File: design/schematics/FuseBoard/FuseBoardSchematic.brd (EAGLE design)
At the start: 114.3 x 88.9 mm, 11 parts

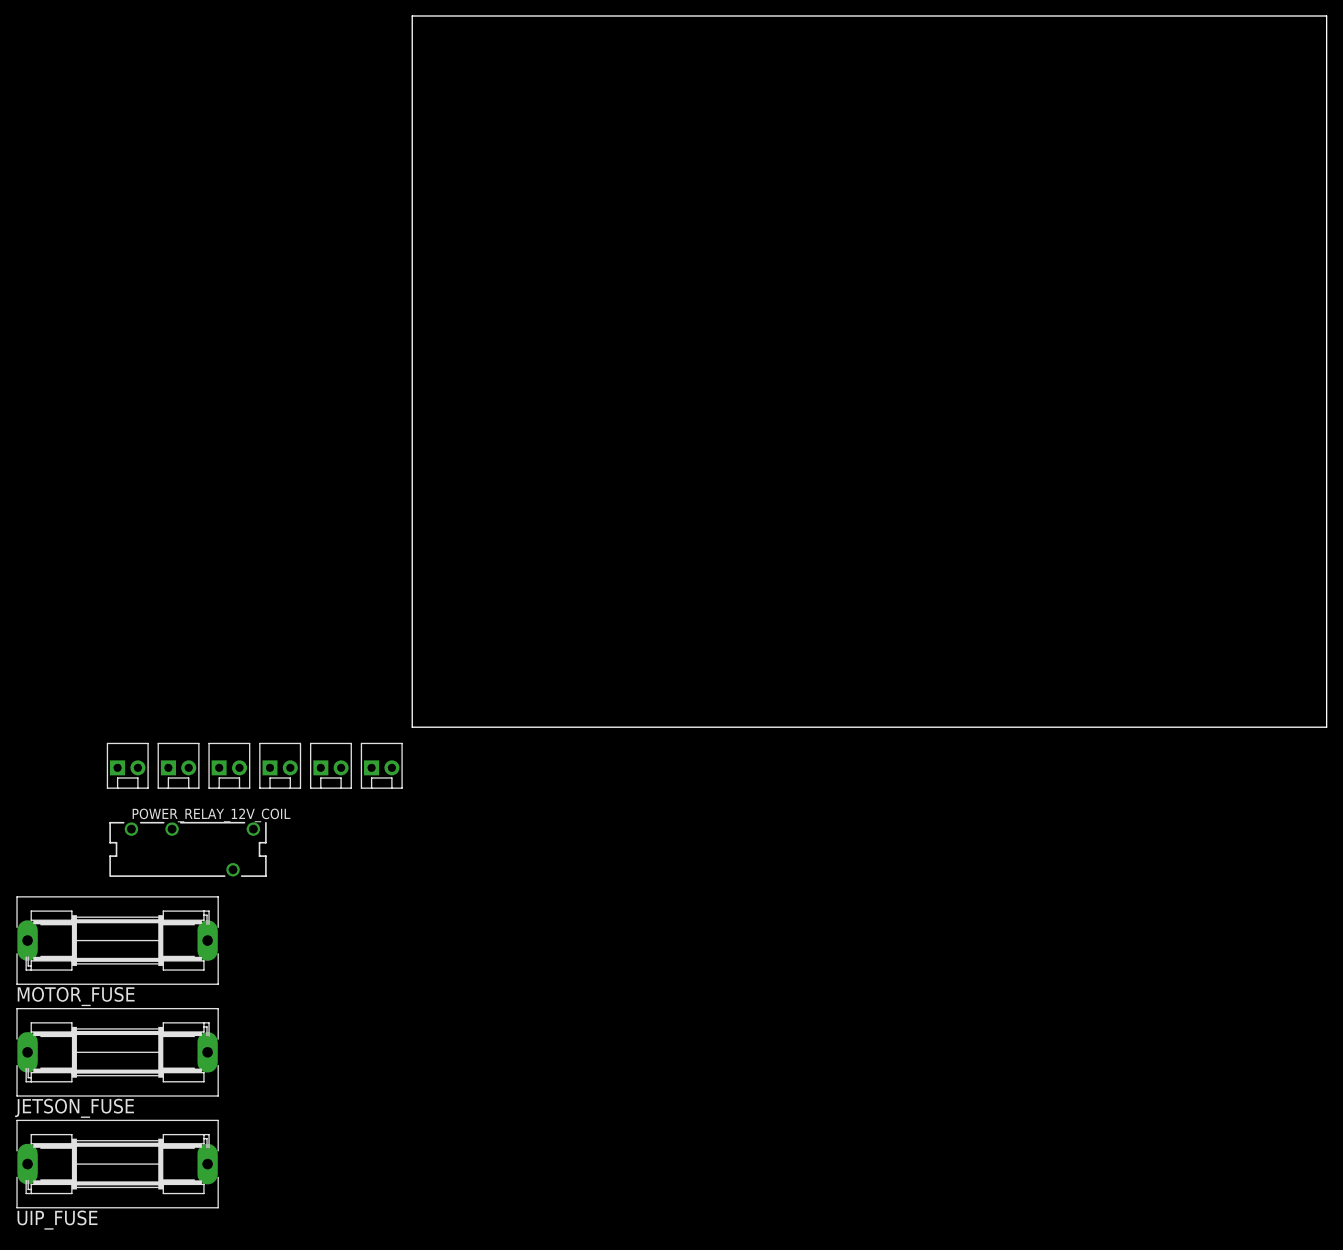
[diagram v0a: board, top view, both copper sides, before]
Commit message: Routed Fuse Board
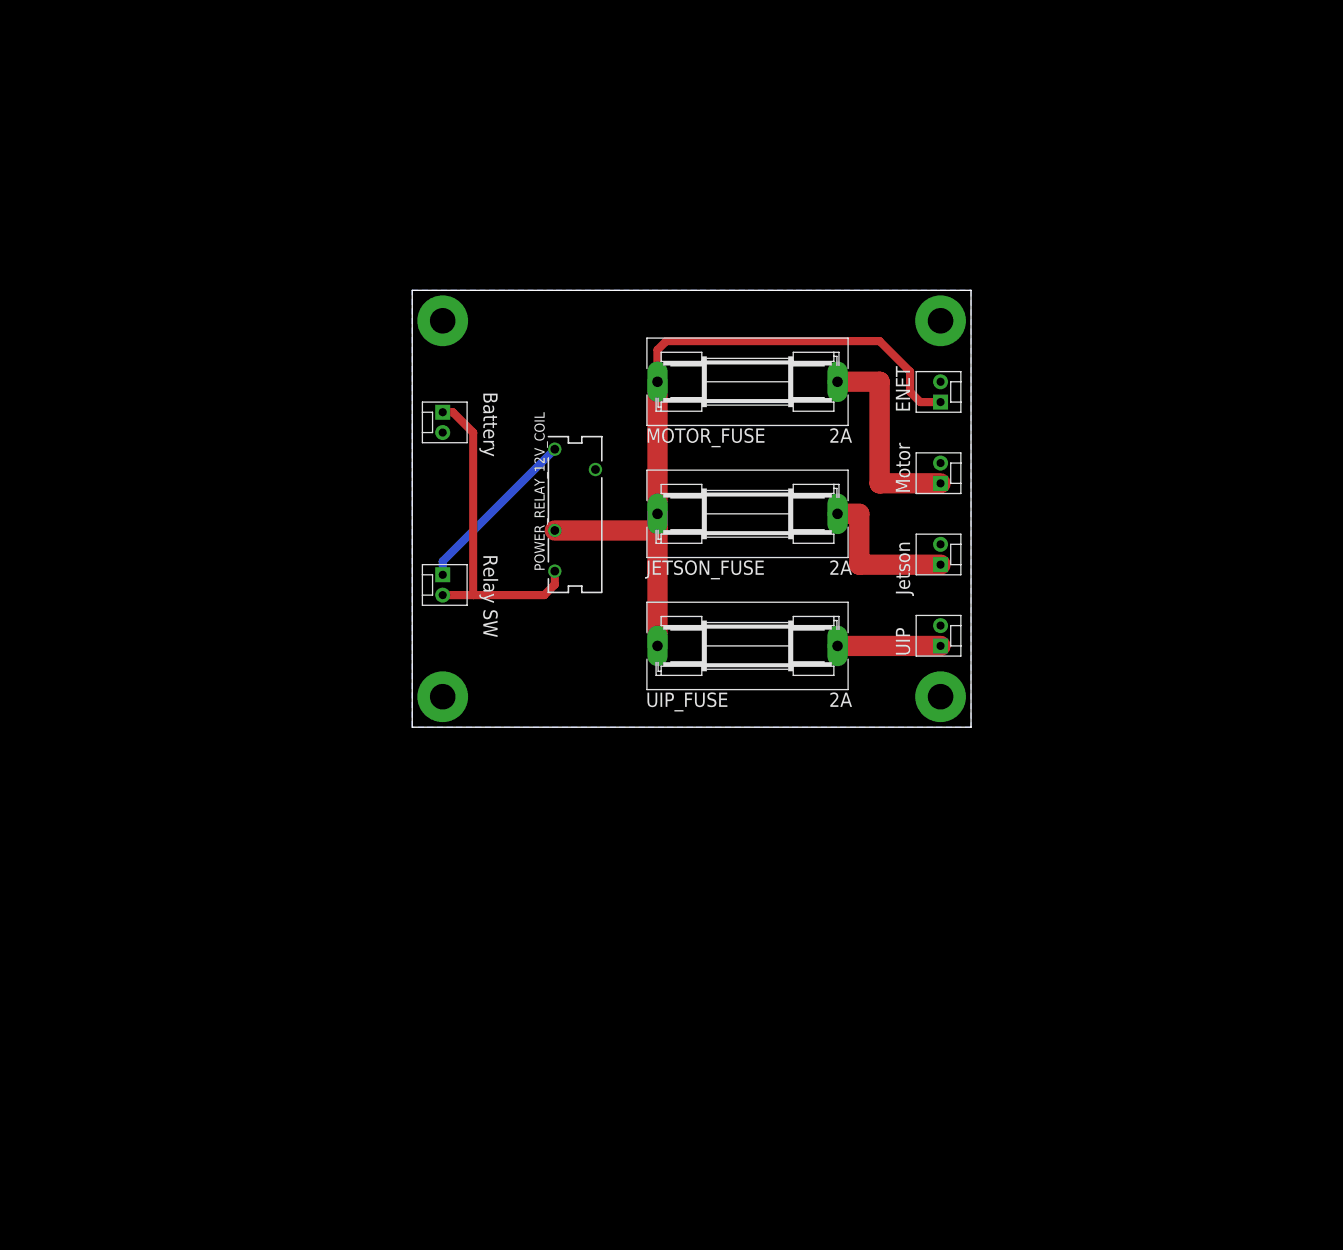
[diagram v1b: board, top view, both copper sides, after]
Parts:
- added S1, S2, S3, S4: STANDOFF_ELECTRICAL, SparkFun-Electromechanical:STANDOFF-ELECTRICAL
- moved MOTOR_FUSE 105.3 mm to (41.9, 43.2)
- moved JETSON_FUSE 103.6 mm to (41.9, 26.7)
- moved UIP_FUSE 102.0 mm to (41.9, 10.2)
- moved UIP 97.7 mm to (66.0, 10.2), turned to 90 degrees
- moved ETHERNET_SWITCH 95.5 mm to (66.0, 40.6), turned to 90 degrees
- moved JETSON 93.7 mm to (66.0, 20.3), turned to 90 degrees
- moved MOTOR_CONTROLLER 85.2 mm to (66.0, 30.5), turned to 90 degrees
- moved POWER_RELAY_12V_COIL 63.9 mm to (20.3, 26.7), turned to 90 degrees
- moved POWER_SWITCH 47.3 mm to (3.81, 19.1), turned to 270 degrees
- moved BATTERY_IN 45.3 mm to (3.81, 39.4), turned to 270 degrees
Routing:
- net 12V_NO_FUSE: track 0.00 -> 92.4 mm
- net 12V_IN: track 0.00 -> 41.4 mm
- net MOTOR_12V: track 0.00 -> 25.6 mm
- net N$2: track 0.00 -> 21.5 mm
- net JETSON_12V: track 0.00 -> 19.2 mm
- net UIP_12V: track 0.00 -> 12.9 mm
- added copper zone on layer 16, net GND
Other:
- board size 114.3 x 88.9 mm -> 69.8 x 54.6 mm
- board text added: "Battery"
- board text added: "ENET"
- board text added: "Jetson"
- board text added: "Motor"
- board text added: "Relay SW"
- board text added: "UIP"

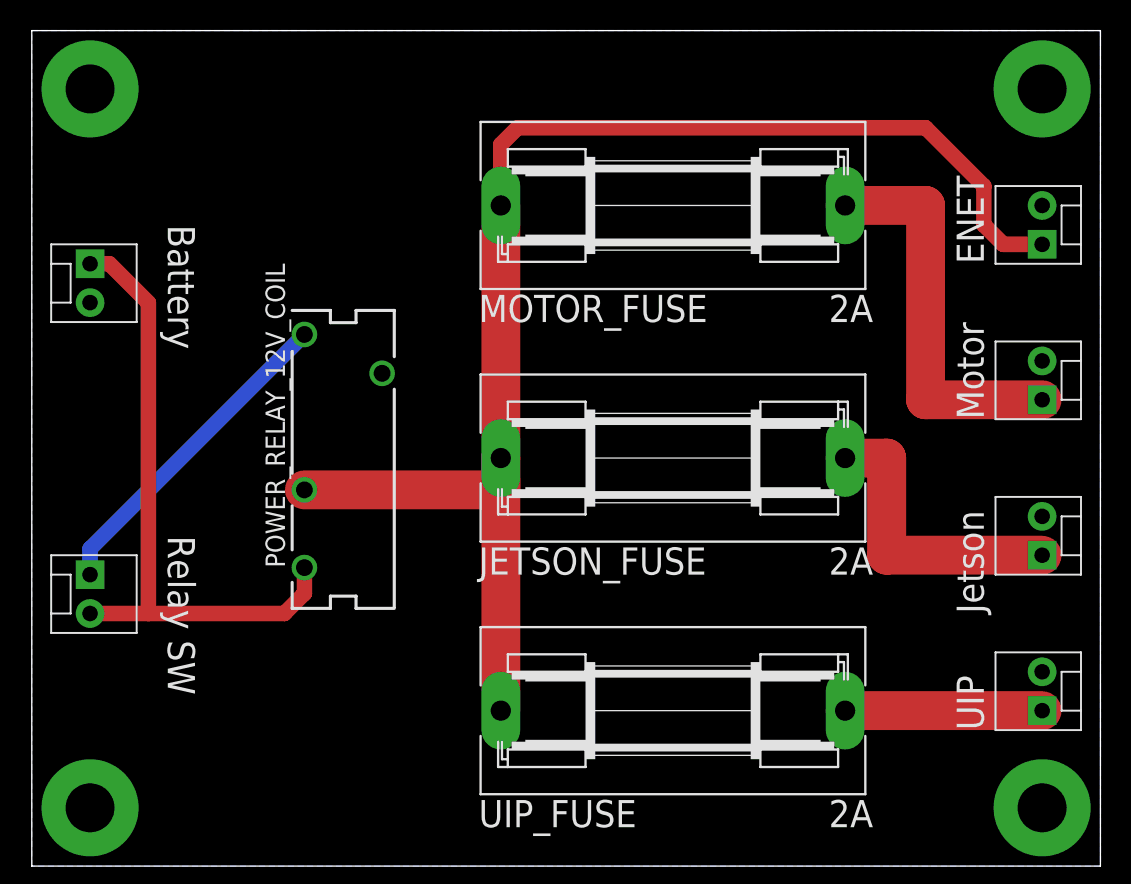
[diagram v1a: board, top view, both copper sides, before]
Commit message: Fixed routing issues and updated BOM
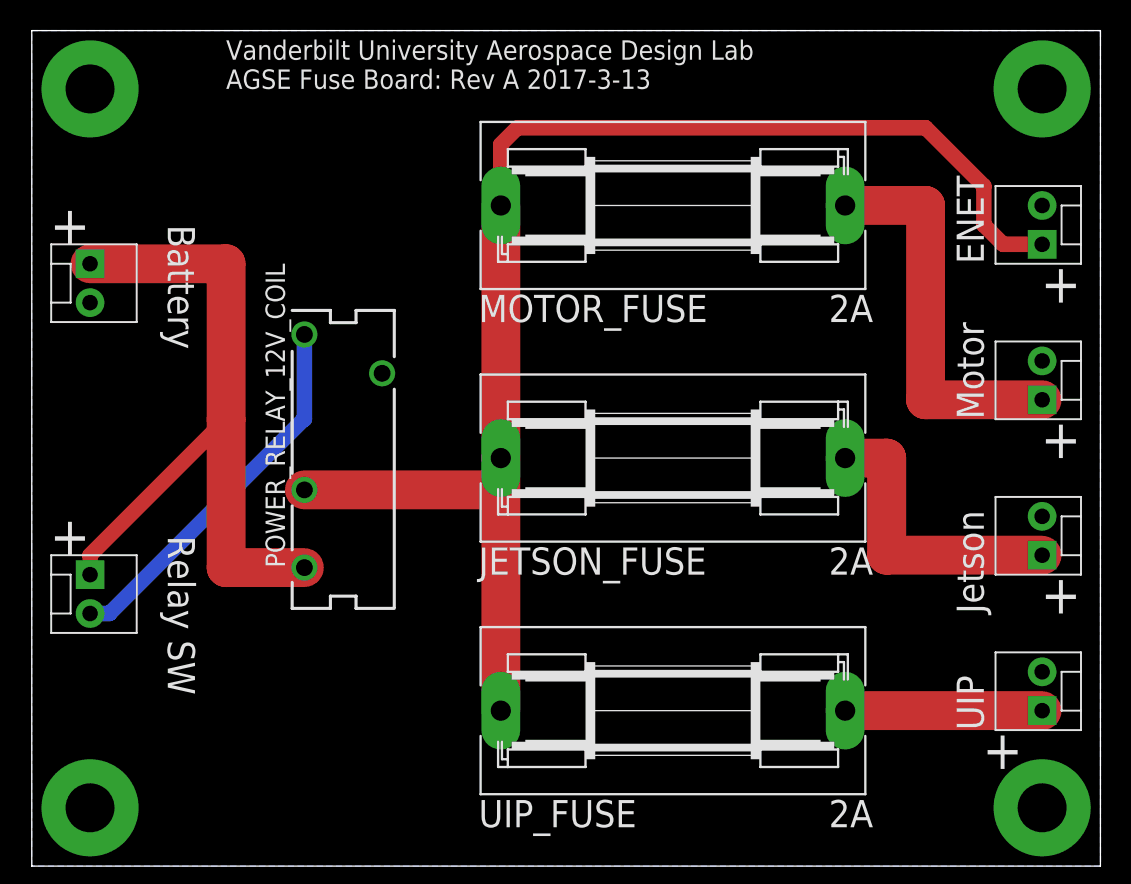
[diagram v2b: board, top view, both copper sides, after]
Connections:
- net 12V_IN: now also POWER_SWITCH.1; no longer POWER_SWITCH.2
- net N$2: now also POWER_SWITCH.2; no longer POWER_SWITCH.1
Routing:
- net 12V_IN: track 41.4 -> 47.7 mm
- net N$2: track 21.5 -> 24.9 mm
- net 12V_NO_FUSE: track 92.4 -> 90.3 mm
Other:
- board text added: "+"
- board text added: "Vanderbilt University Aerospace Design Lab AGSE Fuse Board: Rev A 2017-3-13"

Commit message: Updated fuse ratings
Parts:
- MOTOR_FUSE: value 2A -> 3A
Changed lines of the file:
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@@
 <attribute name="OC_NEWARK" value="unknown" x="20.32" y="26.67" size="1.778" layer="27" rot="R90" display="off"/>
 </element>
-<element name="MOTOR_FUSE" library="fuse" package="SH22,5A" value="2A" x="41.91" y="43.18" smashed="yes">
+<element name="MOTOR_FUSE" library="fuse" package="SH22,5A" value="3A" x="41.91" y="43.18" smashed="yes">
 <attribute name="OC_FARNELL" value="unknown" x="41.91" y="43.18" size="1.778" layer="27" display="off"/>
 <attribute name="MF" value="" x="41.91" y="43.18" size="1.778" layer="27" display="off"/>

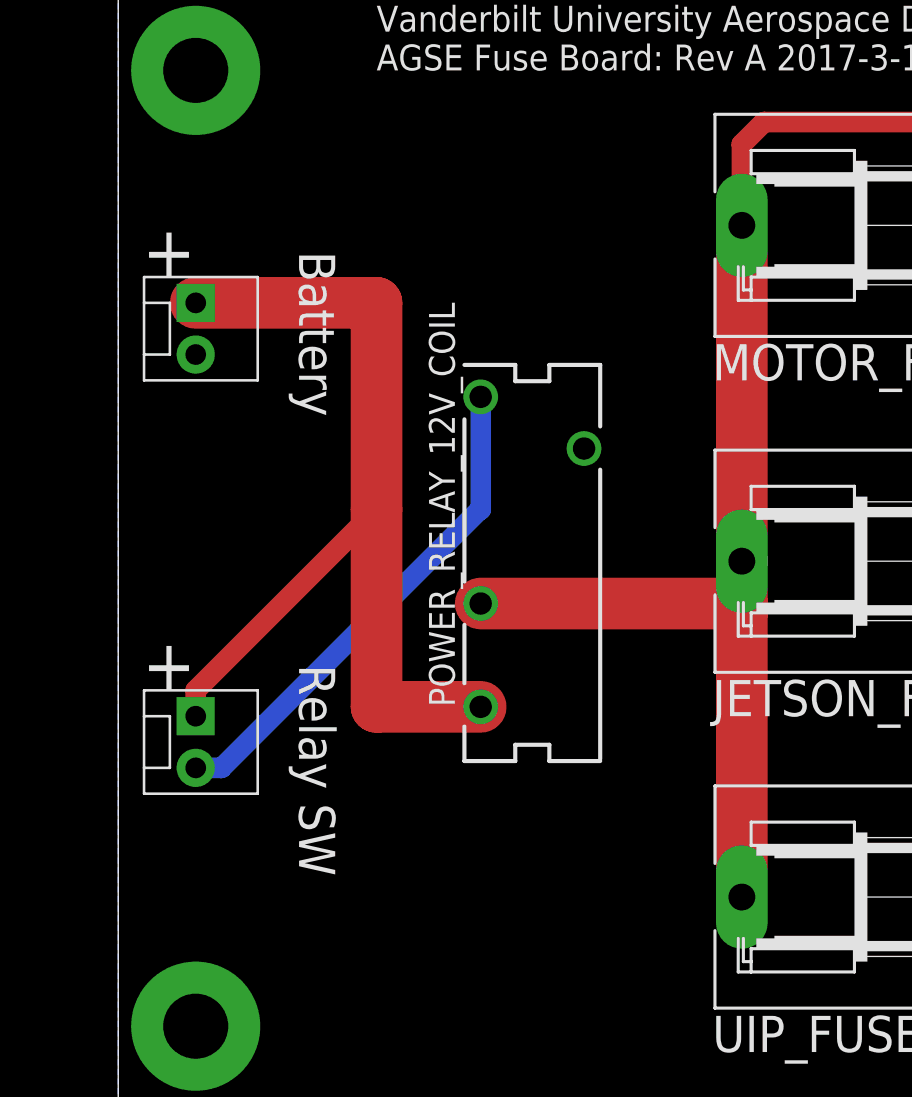
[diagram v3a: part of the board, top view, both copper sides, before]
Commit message: Added wall power port to fuse board
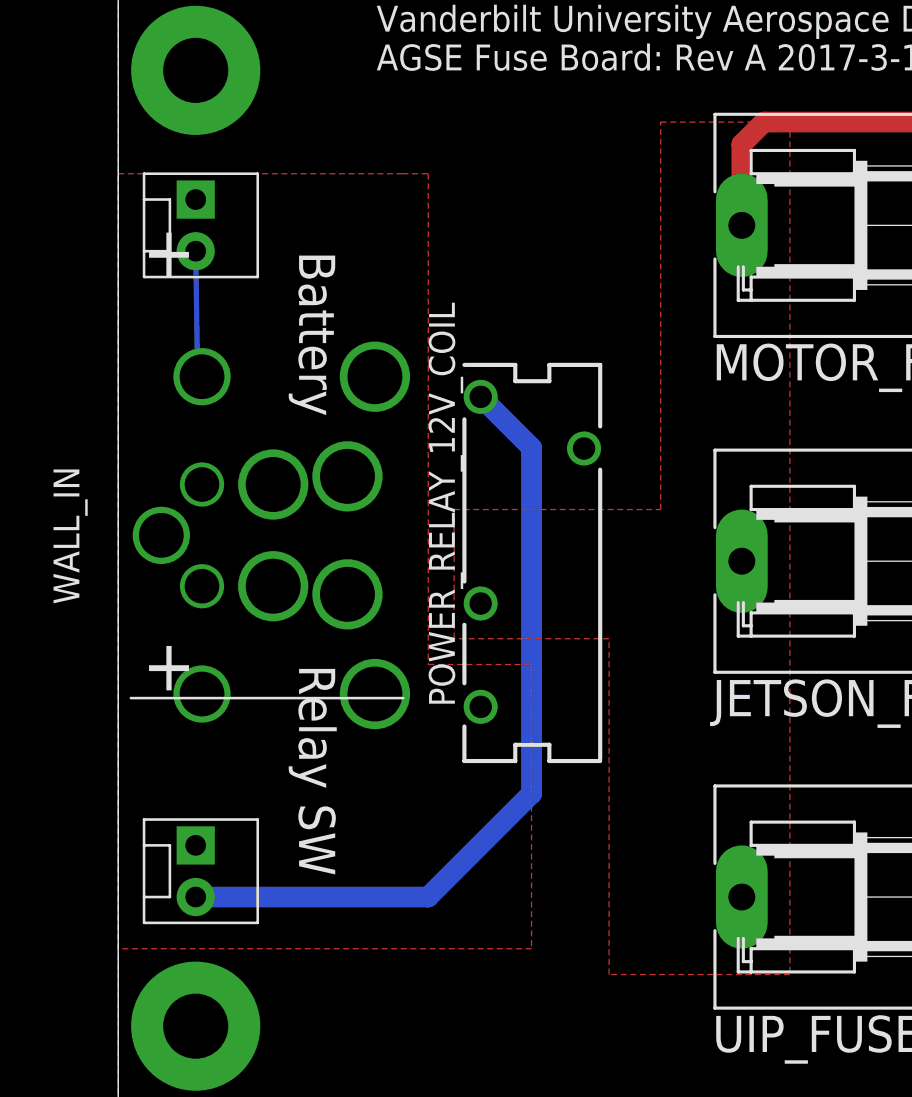
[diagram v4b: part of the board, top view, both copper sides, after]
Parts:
- added WALL_IN: KPJX-4S-S, KPJX:KPJX-4S-S
- moved POWER_SWITCH 6.35 mm to (3.81, 12.7)
- moved BATTERY_IN 5.08 mm to (3.81, 44.5)
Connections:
- net 12V_IN: now also WALL_IN.1, WALL_IN.4
- net GND: now also WALL_IN.2, WALL_IN.3
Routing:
- net 12V_IN: track 47.7 -> 0.00 mm
- net 12V_NO_FUSE: track 90.3 -> 44.5 mm
- net N$2: track 24.9 -> 39.2 mm
- net GND: track 0.13 -> 5.15 mm
- added copper zone on layer 1, net 12V_IN
- added copper zone on layer 1, net 12V_NO_FUSE
